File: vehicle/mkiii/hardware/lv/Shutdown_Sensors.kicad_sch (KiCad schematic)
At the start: 6 parts, among them Q4 SSM3K333R,LF

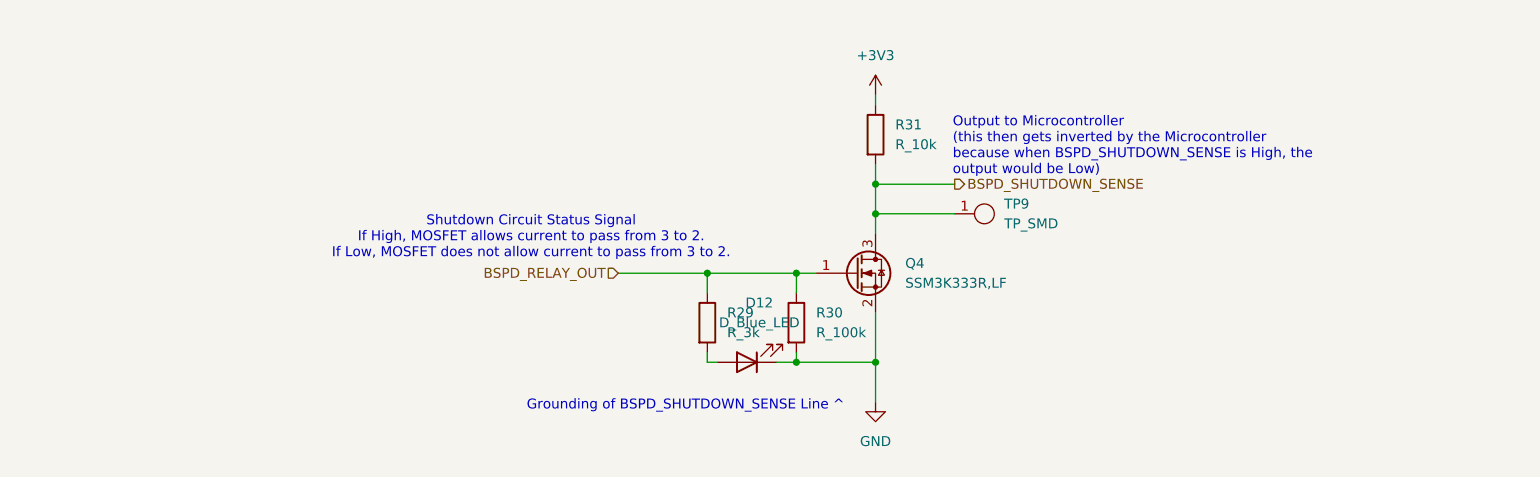
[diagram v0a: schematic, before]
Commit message: Updated title blocks in schematic sheets to include author, set sheet titles, and merged throttle and brake shutdown sense sheets into a single sheet - Shutdown_Sensors.kicad_sch.
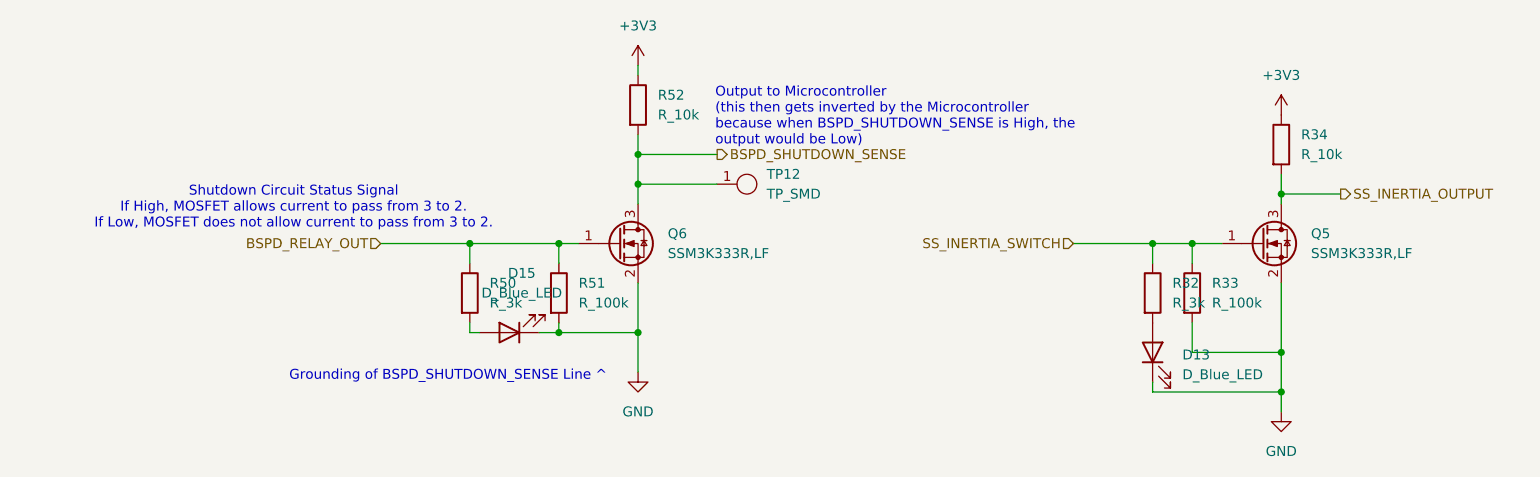
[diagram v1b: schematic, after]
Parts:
- removed D12: D_Blue_LED, OEM:D_0805_2012Metric, symbol OEM:D_LED_Blue_0805
- removed Q4: SSM3K333R,LF, OEM:SOT-23-3, symbol OEM:Q_NMOS_30V_6A_SOT-23F
- removed R29: R_3k, OEM:R_0603_1608Metric, symbol OEM:R_3k_0.1W_0603
- removed R30: R_100k, OEM:R_0603_1608Metric, symbol OEM:R_100k_0.1W_0603
- removed R31: R_10k, OEM:R_0603_1608Metric, symbol OEM:R_10k_0.1W_0603
- removed TP9: TP_SMD, OEM:TP_Hook_SMD, symbol OEM:TP_Hook_SMD
- added D13, D15: D_Blue_LED, OEM:D_0805_2012Metric, symbol OEM:D_LED_Blue_0805
- added Q5, Q6: SSM3K333R,LF, OEM:SOT-23-3, symbol OEM:Q_NMOS_30V_6A_SOT-23F
- added R32, R50: R_3k, OEM:R_0603_1608Metric, symbol OEM:R_3k_0.1W_0603
- added R33, R51: R_100k, OEM:R_0603_1608Metric, symbol OEM:R_100k_0.1W_0603
- added R34, R52: R_10k, OEM:R_0603_1608Metric, symbol OEM:R_10k_0.1W_0603
- added TP12: TP_SMD, OEM:TP_Hook_SMD, symbol OEM:TP_Hook_SMD
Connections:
- net +3V3: now also R34.1, R52.1
- net BSPD_RELAY_OUT: now also Q6.1 (G), R50.1, R51.1
- net BSPD_SHUTDOWN_SENSE: now also Q6.3 (D), R52.2, TP12.1
- net GND: now also D13.1 (K), D15.1 (K), Q5.2 (S), Q6.2 (S), R33.2, R51.2
- new net: D13.2 (A), R32.2
- new net: D15.2 (A), R50.2
- new net SS_INERTIA_OUTPUT: Q5.3 (D), R34.2
- new net SS_INERTIA_SWITCH: Q5.1 (G), R32.1, R33.1
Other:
- title: (none) -> Shutdown Sensors (Throttle & Brake)
